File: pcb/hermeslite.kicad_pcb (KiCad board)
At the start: 4 copper layers, 48.8 x 51 mm, 71 parts, among them CN1 MEC6-140_CONNECTOR_BEMICRO, CN2 PCIE, P1 CONN_4, P10 CONN_1, P13 CONN_1, P14 CONN_1, P15 Si510 73.728, P16 CONN_3X2, P17 CONN_4, P18 CONN_1, P19 CONN_1, P2 CONN_1, P20 CONN_1, P22 CONN_1, P23 CONN_5, P24 CONN_5, P25 CONN_5, P3 CONN_1, P4 CONN_1, P5 CONN_1, P6 CONN_1, P8 CONN_1, P9 CONN_1, T1 TRANSF_ADT8, T2 TRANSF_ADT2, T3 TRANSF_ADT2, U1 AD9866BCPZ, U2 NCP1117ST33T3G, U3 NCP1117ST33T3G

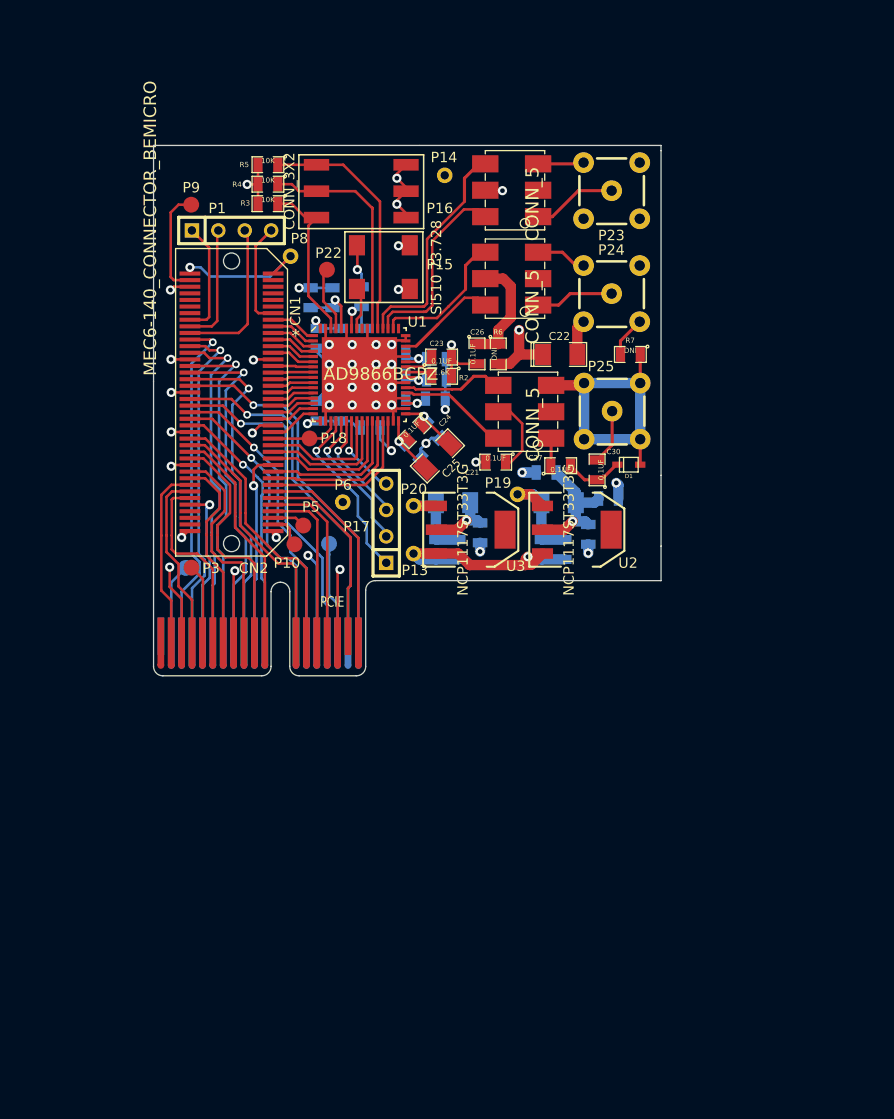
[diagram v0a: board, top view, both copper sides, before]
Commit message: RTL cleanup and upgrade to Quartus 14.0
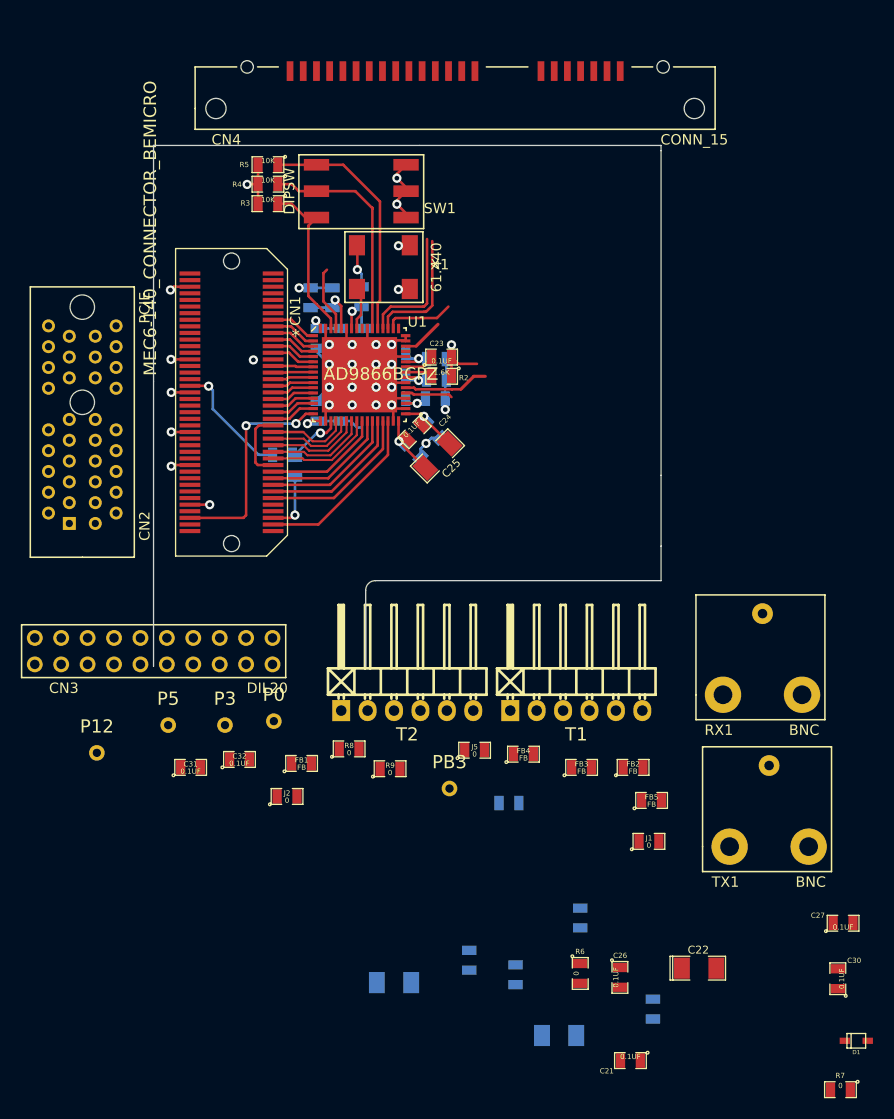
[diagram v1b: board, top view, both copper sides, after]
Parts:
- removed L1, L2, L3, L4: FB, SMD_Packages:SM0805
- removed P1, P17: CONN_4, Connect:SIL-4
- removed P10, P18, P2, P22, P4, P9: CONN_1, Measurement_Points:Measurement_Point_Round-SMD-Pad_Small
- removed P13, P14, P19, P20, P6, P8: CONN_1, Measurement_Points:Measurement_Point_Round-TH_Small
- removed P23, P24, P25: CONN_5, BEMICRO:SMA
- removed T3: TRANSF_ADT2, MINICKTS:minicircuits-CD542
- removed U2, U3: NCP1117ST33T3G, SMD_Packages:SOT223
- added C31: 0.1UF, SMD_Packages:SMD-0805, F.Cu at (104.3, 143.3)
- added C32: 0.1UF, SMD_Packages:SMD-0805, F.Cu at (109.0, 142.5)
- added CN3: DIL20, HERMESLITE:WAVESHARE, F.Cu at (89.3, 133.3)
- added CN4: CONN_15, HERMESLITE:SATA22, F.Cu at (129.7, 79.9)
- added FB1: FB, SMD_Packages:SMD-0805, F.Cu at (114.9, 142.9)
- added FB2: FB, SMD_Packages:SMD-0805, F.Cu at (146.8, 143.3)
- added FB3: FB, SMD_Packages:SMD-0805, F.Cu at (141.9, 143.3)
- added FB4: FB, SMD_Packages:SMD-0805, F.Cu at (136.3, 142.0)
- added FB5: FB, SMD_Packages:SMD-0805, F.Cu at (148.6, 146.4)
- added J1: 0, SMD_Packages:SMD-0805, F.Cu at (148.3, 150.4)
- added J2: 0, SMD_Packages:SMD-0805, F.Cu at (113.5, 146.1)
- added J3: 0, SMD_Packages:SMD-0805, B.Cu at (114.3, 114.4)
- added J4: 0, SMD_Packages:SMD-0805, B.Cu at (113.1, 113.2)
- added J5: 0, SMD_Packages:SMD-0805, F.Cu at (131.6, 141.6)
- added P0: CONN_1, Measurement_Points:Measurement_Point_Round-TH_Small, F.Cu at (112.3, 138.8)
- added P12: CONN_1, Measurement_Points:Measurement_Point_Round-TH_Small, F.Cu at (95.2, 141.9)
- added PB3: CONN_1, Measurement_Points:Measurement_Point_Round-TH_Small, F.Cu at (129.2, 145.3)
- added R8: 0, SMD_Packages:SMD-0805, F.Cu at (119.5, 141.5)
- added R9: 0, SMD_Packages:SMD-0805, F.Cu at (123.4, 143.4)
- added RX1: BNC, HERMESLITE:BNCRA, F.Cu at (159.3, 136.3)
- added TX1: BNC, HERMESLITE:BNCRA, F.Cu at (159.9, 150.9)
- CN2: footprint Connect:PCI-EXPRESS -> HERMESLITE:PCIE36
- P3, P5: footprint Measurement_Points:Measurement_Point_Round-SMD-Pad_Small -> Measurement_Points:Measurement_Point_Round-TH_Small
- R1: value 10K -> 200
- R6, R7: value DNI -> 0
- SW1: renamed from P16; value CONN_3X2 -> DIPSW
- T1: value TRANSF_ADT8 -> 8:1; footprint MINICKTS:minicircuits-CD542 -> Pin_Headers:Pin_Header_Angled_1x06
- T2: value TRANSF_ADT2 -> 4:1; footprint MINICKTS:minicircuits-CD542 -> Pin_Headers:Pin_Header_Angled_1x06
- X1: renamed from P15; value Si510 73.728 -> 61.440
- moved R7 73.5 mm to (166.8, 174.2)
- moved C26 61.5 mm to (145.5, 163.4)
- moved C22 60.5 mm to (153.2, 162.6)
- moved R6 60.1 mm to (141.7, 163.1)
- moved D1 59.6 mm to (168.3, 169.5)
- moved C21 59.0 mm to (146.6, 171.4)
- moved C30 54.1 mm to (166.5, 163.6)
- moved C27 51.7 mm to (167.0, 158.2)
- moved C19 51.2 mm to (139.7, 169.0)
- moved T2 49.5 mm to (125.1, 137.8), turned to 0 degrees
- moved C20 46.5 mm to (123.8, 164.0)
- moved C17 45.0 mm to (148.7, 166.5)
- moved C15 41.0 mm to (135.5, 163.2)
- moved C16 39.6 mm to (131.1, 161.8)
- moved R1 38.5 mm to (134.9, 146.7)
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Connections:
- C10 pad 2: GND -> Net-(C10-Pad2)
- C13 pad 2: GND -> Net-(C10-Pad2)
- C15 pad 1: VIN -> 3VIN
- C16 pad 1: VIN -> 3VIN
- C17 pad 1: VIN -> 3VIN
- C18 pad 1: VIN -> 3VIN
- C19 pad 1: Net-(C19-Pad1) -> 3VIN
- C20 pad 1: Net-(C20-Pad1) -> 3VIN
- C22 pad 1: VIN -> Net-(C22-Pad1)
- C23 pad 1: Net-(C23-Pad1) -> GND
- C23 pad 2: GND -> Net-(C23-Pad2)
- C28 pad 1: Net-(C24-Pad1) -> Net-(C24-Pad2)
- C29 pad 1: Net-(C24-Pad2) -> Net-(C24-Pad1)
- CN1 pad 78: Net-(CN1-Pad78) -> DVDD
- CN1 pad 79: Net-(CN1-Pad79) -> 5VIN
- CN1 pad 80: Net-(CN1-Pad79) -> 5VIN
- CN2 pad A1: Net-(CN2-PadA1) -> GND
- CN2 pad A11: Net-(CN1-Pad34) -> 12VIN
- CN2 pad A12: Net-(CN1-Pad36) -> 5VIN
- CN2 pad A13: Net-(CN1-Pad38) -> 3VIN
- CN2 pad A14: GND -> Net-(CN1-Pad66)
- CN2 pad A15: Net-(CN1-Pad40) -> Net-(CN1-Pad64)
- CN2 pad A16: Net-(CN2-PadA16) -> Net-(CN1-Pad62)
- CN2 pad A17: Net-(CN1-Pad42) -> Net-(CN1-Pad60)
- CN2 pad A18: Net-(CN1-Pad46) -> GND
- CN2 pad A2: Net-(CN2-PadA2) -> RXN
- CN2 pad A3: Net-(CN1-Pad60) -> RXP
- CN2 pad A4: Net-(CN1-Pad58) -> GND
- CN2 pad A5: GND -> TXN
- CN2 pad A6: Net-(CN1-Pad56) -> TXP
- CN2 pad A7: Net-(CN1-Pad52) -> GND
- CN2 pad A8: Net-(CN1-Pad50) -> TXLN
- CN2 pad A9: Net-(CN1-Pad48) -> TXLP
- CN2 pad B1: Net-(CN2-PadB1) -> GND
- CN2 pad B10: Net-(CN1-Pad24) -> GND
- CN2 pad B11: Net-(CN1-Pad26) -> 12VIN
- CN2 pad B12: Net-(CN1-Pad28) -> 5VIN
- CN2 pad B13: Net-(CN1-Pad30) -> 3VIN
- CN2 pad B14: Net-(CN1-Pad7) -> Net-(CN1-Pad50)
- CN2 pad B15: Net-(CN1-Pad9) -> Net-(CN1-Pad52)
- CN2 pad B16: GND -> Net-(CN1-Pad56)
- CN2 pad B17: Net-(CN1-Pad11) -> Net-(CN1-Pad58)
- CN2 pad B18: Net-(CN1-Pad13) -> GND
- CN2 pad B2: Net-(CN1-Pad16) -> GND
- CN2 pad B4: Net-(CN1-Pad14) -> GND
- CN2 pad B5: Net-(CN2-PadB5) -> GND
- CN2 pad B6: Net-(CN1-Pad12) -> GND
- CN2 pad B7: Net-(CN1-Pad18) -> GND
- CN2 pad B9: Net-(CN1-Pad20) -> GND
- D1 pad 1: Net-(D1-Pad1) -> GND
- P3 pad 1: Net-(CN2-PadB5) -> 3VIN
- P5 pad 1: Net-(CN1-Pad5) -> 5VIN
- R1 pad 1: DVDD -> TXP
- R1 pad 2: Net-(R1-Pad2) -> TXN
- R2 pad 1: GND -> Net-(R2-Pad1)
- R2 pad 2: Net-(R2-Pad2) -> GND
- R3 pad 1: Net-(P16-Pad2) -> Net-(R3-Pad1)
- R4 pad 1: Net-(P16-Pad4) -> Net-(R4-Pad1)
- R5 pad 1: Net-(P16-Pad6) -> Net-(R5-Pad1)
- R6 pad 2: VIN -> Net-(C22-Pad1)
- R7 pad 1: Net-(D1-Pad1) -> DVDD
- R7 pad 2: GND -> Net-(R5-Pad1)
- SW1 pad 1: DVDD -> Net-(R5-Pad1)
- SW1 pad 2: Net-(P16-Pad2) -> DVDD
- SW1 pad 3: DVDD -> Net-(R4-Pad1)
- SW1 pad 4: Net-(P16-Pad4) -> DVDD
- SW1 pad 5: DVDD -> Net-(R3-Pad1)
- SW1 pad 6: Net-(P16-Pad6) -> DVDD
- T1 pad 3: Net-(D1-Pad1) -> GND
- T1 pad 4: RXP -> Net-(C32-Pad1)
- T1 pad 6: RXN -> Net-(C31-Pad1)
- T2 pad 4: Net-(T2-Pad4) -> TXP
- T2 pad 5: GND -> Net-(C26-Pad1)
- T2 pad 6: Net-(T2-Pad6) -> TXN
- U1 pad 16: Net-(CN1-Pad31) -> Net-(CN1-Pad6)
- U1 pad 19: Net-(CN1-Pad29) -> Net-(J3-Pad1)
- U1 pad 20: SDIO -> Net-(CN1-Pad31)
- U1 pad 21: SDO -> Net-(CN1-Pad29)
- U1 pad 22: SCLK -> Net-(CN1-Pad27)
- U1 pad 23: SEN -> Net-(CN1-Pad25)
- U1 pad 24: Net-(CN1-Pad27) -> Net-(CN1-Pad23)
- U1 pad 25: Net-(CN1-Pad25) -> Net-(CN1-Pad19)
- U1 pad 26: Net-(CN1-Pad23) -> Net-(CN1-Pad17)
- U1 pad 27: Net-(CN1-Pad19) -> Net-(CN1-Pad15)
- U1 pad 28: Net-(CN1-Pad17) -> Net-(CN1-Pad13)
- U1 pad 29: Net-(CN1-Pad15) -> Net-(CN1-Pad11)
- U1 pad 30: Net-(R1-Pad2) -> Net-(CN1-Pad3)
- U1 pad 32: Net-(C24-Pad2) -> Net-(C24-Pad1)
- U1 pad 33: Net-(C24-Pad1) -> Net-(C24-Pad2)
- U1 pad 41: Net-(R2-Pad2) -> Net-(R2-Pad1)
- U1 pad 42: Net-(C23-Pad1) -> Net-(C23-Pad2)
- U1 pad 46: Net-(T3-Pad6) -> TXN
- U1 pad 50: Net-(T3-Pad4) -> TXP
- U1 pad 51: Net-(T2-Pad6) -> TXLN
- U1 pad 52: Net-(T2-Pad4) -> TXLP
- U1 pad 53: Net-(P16-Pad6) -> Net-(R5-Pad1)
- U1 pad 54: Net-(P16-Pad4) -> Net-(R4-Pad1)
- U1 pad 62: Net-(P16-Pad2) -> Net-(R3-Pad1)
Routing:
- net GND: track 281.2 -> 173.8 mm, vias 38 -> 28
- net Net-(CN1-Pad42): track 34.2 -> 0.00 mm, vias 1 -> 0
- net Net-(CN1-Pad50): track 33.1 -> 0.00 mm, vias 1 -> 0
- net Net-(CN1-Pad60): track 33.0 -> 0.00 mm, vias 1 -> 0
- net Net-(CN1-Pad52): track 32.8 -> 0.00 mm, vias 1 -> 0
- net Net-(CN1-Pad58): track 32.7 -> 0.00 mm, vias 1 -> 0
- net DVDD: track 24.4 -> 57.1 mm, vias 6 -> 3
- net Net-(CN1-Pad56): track 32.6 -> 0.00 mm, vias 1 -> 0
- net Net-(CN1-Pad40): track 32.4 -> 0.00 mm, vias 1 -> 0
- net Net-(CN1-Pad48): track 32.1 -> 0.00 mm, vias 1 -> 0
- net Net-(D1-Pad1): track 30.1 -> 0.00 mm
- net VIN: track 29.4 -> 0.00 mm, vias 2 -> 0
- net Net-(CN1-Pad38): track 28.3 -> 0.00 mm, vias 1 -> 0
- net Net-(CN1-Pad36): track 27.5 -> 0.00 mm, vias 1 -> 0
- net Net-(CN1-Pad30): track 26.0 -> 0.00 mm
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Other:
- board size 48.8 x 51 mm -> 48.8 x 50.1 mm

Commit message: Intermediate save before move of PCIe connector
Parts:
- removed CN3: DIL20, HERMESLITE:WAVESHARE
- removed R6, R7: 0, SMD_Packages:SM0805
- removed R8, R9: 0, SMD_Packages:SMD-0805
- removed SW1: DIPSW, HERMESLITE:DIPSWITCH
- added C33: 0.1UF, SMD_Packages:SMD-0805, B.Cu at (104.8, 108.4)
- added MH: VAL**, HERMESLITE:MH, F.Cu at (116.7, 122.8)
- added MH: VAL**, HERMESLITE:MH, F.Cu at (108.3, 87.1)
- added MH: VAL**, HERMESLITE:MH, F.Cu at (146.7, 87.1)
- added MH: VAL**, HERMESLITE:MH, F.Cu at (146.7, 122.8)
- added TP1: CONN_1, HERMESLITE:TP, F.Cu at (102.1, 108.4)
- added TP2: CONN_1, HERMESLITE:TP, F.Cu at (114.1, 99.3)
- added U2: EEPROM, SMD_Packages:SOT-23-6, B.Cu at (105.1, 111.9)
- C15, C16, C17, C18, R1: footprint SMD_Packages:SM0805 -> SMD_Packages:SMD-0805; moved to F.Cu
- C19, C20: footprint SMD_Packages:SM1206POL -> SMD_Packages:SMD-1206_Pol; moved to F.Cu
- C21, C26, C27, C30: footprint SMD_Packages:SM0805 -> SMD_Packages:SMD-0805; moved to B.Cu
- C22: footprint SMD_Packages:SM1206POL -> SMD_Packages:SMD-1206_Pol; moved to B.Cu
- CN2: footprint HERMESLITE:PCIE36 -> HERMESLITE:PCIESTRADDLE
- CN4: value CONN_15 -> SATA22; moved to B.Cu
- D1, FB5: moved to B.Cu
- R3: value 10K -> 0; footprint SMD_Packages:SM0805 -> SMD_Packages:SMD-0805; moved to B.Cu
- R4, R5: value 10K -> 47; footprint SMD_Packages:SM0805 -> SMD_Packages:SMD-0805; moved to B.Cu
- RX1, TX1: value BNC -> ~; footprint HERMESLITE:BNCRA -> HERMESLITE:RFSTRADDLE; moved to B.Cu
- T1, T2: footprint Pin_Headers:Pin_Header_Angled_1x06 -> HERMESLITE:TRANSF
- moved C22 69.9 mm to (141.0, 93.7)
- moved C26 66.9 mm to (141.2, 96.7), turned to 90 degrees
- moved C21 65.3 mm to (142.4, 106.3), turned to 90 degrees
- moved D1 65.0 mm to (142.4, 109.9), turned to 90 degrees
- moved C30 55.8 mm to (143.3, 112.8), turned to 0 degrees
- moved TX1 55.1 mm to (147.8, 97.1)
- moved FB5 54.1 mm to (136.4, 93.7)
- moved J1 54.0 mm to (129.0, 100.0), turned to 270 degrees
- moved C27 52.3 mm to (139.1, 114.0)
- moved CN4 51.9 mm to (125.7, 131.6), turned to 180 degrees
- moved R1 48.4 mm to (131.0, 98.4), turned to 270 degrees
- moved CN2 48.1 mm to (122.3, 85.3), turned to 0 degrees
- moved P12 47.6 mm to (135.9, 117.1)
- moved J2 47.4 mm to (131.0, 102.0), turned to 270 degrees
- moved C31 44.7 mm to (132.0, 108.2), turned to 180 degrees
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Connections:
- C21 pad 1: Net-(C21-Pad1) -> GND
- C21 pad 2: GND -> Net-(C21-Pad2)
- C31 pad 1: Net-(C31-Pad1) -> RXN
- C31 pad 2: RXN -> Net-(C31-Pad2)
- C32 pad 1: Net-(C32-Pad1) -> RXP
- C32 pad 2: RXP -> Net-(C32-Pad2)
- CN1 pad 10: GND -> Net-(C33-Pad1)
- CN1 pad 22: GND -> Net-(C33-Pad1)
- CN1 pad 32: GND -> Net-(C33-Pad1)
- CN1 pad 4: Net-(CN1-Pad4) -> GND
- CN1 pad 44: GND -> Net-(C33-Pad1)
- CN1 pad 54: GND -> Net-(C33-Pad1)
- CN1 pad 76: GND -> Net-(C33-Pad1)
- CN2 pad A12: 5VIN -> 12VIN
- CN2 pad A13: 3VIN -> 5VIN
- CN2 pad A14: Net-(CN1-Pad66) -> 5VIN
- CN2 pad A15: Net-(CN1-Pad64) -> 3VIN
- CN2 pad A16: Net-(CN1-Pad62) -> 3VIN
- CN2 pad A17: Net-(CN1-Pad60) -> GND
- CN2 pad A2: RXN -> GND
- CN2 pad A3: RXP -> GND
- CN2 pad A5: TXN -> GND
- CN2 pad A6: TXP -> GND
- CN2 pad A8: TXLN -> GND
- CN2 pad A9: TXLP -> GND
- CN2 pad B11: 12VIN -> Net-(CN1-Pad50)
- CN2 pad B12: 5VIN -> Net-(CN1-Pad52)
- CN2 pad B13: 3VIN -> Net-(CN1-Pad56)
- CN2 pad B14: Net-(CN1-Pad50) -> Net-(CN1-Pad58)
- CN2 pad B15: Net-(CN1-Pad52) -> Net-(CN1-Pad66)
- CN2 pad B16: Net-(CN1-Pad56) -> Net-(CN1-Pad64)
- CN2 pad B17: Net-(CN1-Pad58) -> Net-(CN1-Pad62)
- CN2 pad B18: GND -> Net-(CN1-Pad60)
- CN2 pad B2: GND -> RXN
- CN2 pad B3: GND -> RXP
- CN2 pad B5: GND -> TXN
- CN2 pad B6: GND -> TXP
- CN2 pad B8: GND -> TXLN
- CN2 pad B9: GND -> TXLP
- CN4 pad P1: (no net) -> 3VIN
- CN4 pad P10: (no net) -> GND
- CN4 pad P11: (no net) -> GND
- CN4 pad P12: (no net) -> GND
- CN4 pad P13: (no net) -> 12VIN
- CN4 pad P14: (no net) -> 12VIN
- CN4 pad P15: (no net) -> 12VIN
- CN4 pad P2: (no net) -> 3VIN
- CN4 pad P3: (no net) -> 3VIN
- CN4 pad P4: (no net) -> GND
- CN4 pad P5: (no net) -> GND
- CN4 pad P6: (no net) -> GND
- CN4 pad P7: (no net) -> 5VIN
- CN4 pad P8: (no net) -> 5VIN
- CN4 pad P9: (no net) -> 5VIN
- CN4 pad S1: (no net) -> GND
- CN4 pad S2: (no net) -> Net-(CN1-Pad12)
- CN4 pad S3: (no net) -> Net-(CN1-Pad14)
- CN4 pad S4: (no net) -> GND
- CN4 pad S5: (no net) -> Net-(CN1-Pad16)
- CN4 pad S6: (no net) -> Net-(CN1-Pad18)
- CN4 pad S7: (no net) -> GND
- D1 pad 1: GND -> Net-(C27-Pad2)
- D1 pad 2: Net-(C27-Pad2) -> GND
- J5 pad 1: Net-(CN1-Pad4) -> GND
- R3 pad 1: Net-(R3-Pad1) -> Net-(C26-Pad1)
- R3 pad 2: GND -> Net-(C22-Pad1)
- R4 pad 1: Net-(R4-Pad1) -> Net-(CN1-Pad6)
- R5 pad 1: Net-(R5-Pad1) -> GND
- R5 pad 2: GND -> Net-(J3-Pad1)
- T1 pad 2: (no net) -> Net-(C21-Pad2)
- T1 pad 4: Net-(C32-Pad1) -> RXP
- T1 pad 5: Net-(C21-Pad1) -> Net-(C21-Pad2)
- T1 pad 6: Net-(C31-Pad1) -> RXN
- T2 pad 2: (no net) -> Net-(C26-Pad1)
- U1 pad 37: RXN -> Net-(C31-Pad2)
- U1 pad 38: RXP -> Net-(C32-Pad2)
- U1 pad 53: Net-(R5-Pad1) -> GND
- U1 pad 54: Net-(R4-Pad1) -> GND
- U1 pad 62: Net-(R3-Pad1) -> GND
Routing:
- net DVDD: track 57.1 -> 17.7 mm, vias 3 -> 4
- net GND: track 173.8 -> 195.1 mm, vias 28 -> 25
- net Net-(CN1-Pad18): track 0.00 -> 19.7 mm, vias 0 -> 1
- net Net-(CN1-Pad16): track 0.00 -> 18.3 mm, vias 0 -> 1
- net Net-(CN1-Pad14): track 0.00 -> 18.2 mm, vias 0 -> 1
- net Net-(C33-Pad1): track 0.00 -> 16.8 mm, vias 0 -> 6
- net Net-(CN1-Pad12): track 0.00 -> 16.4 mm, vias 0 -> 1
- net Net-(R4-Pad1): track 16.1 -> 0.00 mm, vias 1 -> 0
- net Net-(CN1-Pad1): track 0.18 -> 11.2 mm
- net RXP: track 8.24 -> 0.00 mm
- net Net-(R5-Pad1): track 7.81 -> 0.00 mm
- net Net-(CN1-Pad34): track 0.00 -> 7.50 mm, vias 0 -> 1
- net Net-(C31-Pad2): track 0.00 -> 6.58 mm
- net Net-(J2-Pad2): track 0.00 -> 6.55 mm
- net Net-(C32-Pad2): track 0.00 -> 6.50 mm
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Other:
- board size 48.8 x 50.1 mm -> 49.9 x 49.9 mm

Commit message: Commit before silkscreen cleanup
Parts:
- removed D1: CDSOD323, HERMESLITE:SOD323
- removed R3: 0, SMD_Packages:SMD-0805
- removed RX1, TX1: ~, HERMESLITE:RFSTRADDLE
- removed T1: 8:1, HERMESLITE:TRANSF
- removed T2: 4:1, HERMESLITE:TRANSF
- added C34: 0.1UF, SMD_Packages:SMD-0805, B.Cu at (141.2, 90.4)
- added C35: 0.1UF, SMD_Packages:SMD-0805, B.Cu at (137.2, 90.4)
- added C36: 0.1UF, SMD_Packages:SMD-0805, B.Cu at (142.3, 122.5)
- added FB6: FB, SMD_Packages:SMD-0805, B.Cu at (139.5, 96.6)
- added FB7: FB, SMD_Packages:SMD-0805, B.Cu at (137.4, 96.6)
- added FB8: FB, SMD_Packages:SMD-0805, B.Cu at (140.1, 102.1)
- added R6: 200, SMD_Packages:SMD-0805, F.Cu at (128.2, 98.1)
- C21, C26, C27, C30: value 0.1UF -> 1UF
- C22: value 10UF -> 0.1UF; footprint SMD_Packages:SMD-1206_Pol -> SMD_Packages:SMD-0805
- moved C17 32.8 mm to (138.1, 122.0), turned to 90 degrees
- moved C21 31.8 mm to (115.7, 89.1)
- moved CN2 29.9 mm to (146.5, 102.9), turned to 270 degrees
- moved C22 27.6 mm to (113.8, 89.1), turned to 90 degrees
- moved C15 26.9 mm to (136.1, 122.0), turned to 90 degrees
- moved C19 26.0 mm to (140.4, 121.3), turned to 90 degrees
- moved C27 23.9 mm to (135.2, 90.4), turned to 90 degrees
- moved C18 23.4 mm to (123.8, 122.0), turned to 90 degrees
- moved FB5 22.6 mm to (113.8, 93.1), turned to 270 degrees
- moved C20 22.2 mm to (121.5, 121.3), turned to 90 degrees
- moved C16 20.2 mm to (125.8, 122.0), turned to 90 degrees
- moved FB3 11.0 mm to (134.1, 122.0), turned to 90 degrees
- moved C30 10.1 mm to (140.4, 122.5), turned to 90 degrees
- moved P12 9.44 mm to (140.2, 125.5)
- moved C26 6.61 mm to (139.2, 90.4)
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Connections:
- net Net-(CN1-Pad56) renamed /EXP_GPIO1
- net Net-(CN1-Pad58) renamed /EXP_GPIO2
- net RXN renamed /RXN
- net RXP renamed /RXP
- net TXLN renamed /TXLN
- net TXLP renamed /TXLP
- net TXN renamed /TXN
- net TXP renamed /TXP
- C10 pad 2: Net-(C10-Pad2) -> GND
- C13 pad 2: Net-(C10-Pad2) -> GND
- C21 pad 1: GND -> 5VIN
- C21 pad 2: Net-(C21-Pad2) -> GND
- C22 pad 1: Net-(C22-Pad1) -> 5VIN
- C23 pad 1: GND -> Net-(C23-Pad1)
- C23 pad 2: Net-(C23-Pad2) -> GND
- C26 pad 1: Net-(C26-Pad1) -> DVDD
- C27 pad 1: Net-(C27-Pad1) -> 5VIN
- C27 pad 2: Net-(C27-Pad2) -> GND
- C28 pad 1: Net-(C24-Pad2) -> Net-(C24-Pad1)
- C29 pad 1: Net-(C24-Pad1) -> Net-(C24-Pad2)
- C30 pad 1: Net-(C27-Pad2) -> 12VIN
- C30 pad 2: Net-(C30-Pad2) -> GND
- C33 pad 1: Net-(C33-Pad1) -> GND
- CN1 pad 10: Net-(C33-Pad1) -> GND
- CN1 pad 22: Net-(C33-Pad1) -> GND
- CN1 pad 32: Net-(C33-Pad1) -> GND
- CN1 pad 44: Net-(C33-Pad1) -> GND
- CN1 pad 50: Net-(CN1-Pad50) -> /PTT#
- CN1 pad 52: Net-(CN1-Pad52) -> /EXP_GPIO0
- CN1 pad 54: Net-(C33-Pad1) -> GND
- CN1 pad 60: Net-(CN1-Pad60) -> /EXP_SEN
- CN1 pad 62: Net-(CN1-Pad62) -> /EXP_SDI
- CN1 pad 64: Net-(CN1-Pad64) -> /EXP_SDO
- CN1 pad 66: Net-(CN1-Pad66) -> /EXP_SCLK
- CN1 pad 73: Net-(CN1-Pad73) -> /PTT#
- CN1 pad 75: Net-(CN1-Pad75) -> /EXP_GPIO0
- CN1 pad 76: Net-(C33-Pad1) -> GND
- CN1 pad 79: 5VIN -> FPGA5V
- CN1 pad 80: 5VIN -> FPGA5V
- CN2 pad A11: 12VIN -> EXP12V
- CN2 pad A12: 12VIN -> EXP12V
- CN2 pad A13: 5VIN -> EXP5V
- CN2 pad A14: 5VIN -> EXP5V
- CN2 pad A15: 3VIN -> EXP3V
- CN2 pad A16: 3VIN -> EXP3V
- CN2 pad B11: Net-(CN1-Pad50) -> /PTT#
- CN2 pad B12: Net-(CN1-Pad52) -> /EXP_GPIO0
- CN2 pad B15: Net-(CN1-Pad66) -> /EXP_SEN
- CN2 pad B16: Net-(CN1-Pad64) -> /EXP_SDI
- CN2 pad B17: Net-(CN1-Pad62) -> /EXP_SDO
- CN2 pad B18: Net-(CN1-Pad60) -> /EXP_SCLK
- FB5 pad 2: Net-(C22-Pad1) -> FPGA5V
- R2 pad 1: Net-(R2-Pad1) -> GND
- R2 pad 2: GND -> Net-(R2-Pad2)
- U1 pad 32: Net-(C24-Pad1) -> Net-(C24-Pad2)
- U1 pad 33: Net-(C24-Pad2) -> Net-(C24-Pad1)
- U1 pad 41: Net-(R2-Pad1) -> Net-(R2-Pad2)
- U1 pad 42: Net-(C23-Pad2) -> Net-(C23-Pad1)
- U2 pad 2: Net-(C33-Pad1) -> GND
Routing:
- net GND: track 195.1 -> 288.1 mm, vias 25 -> 49
- net 5VIN: track 0.01 -> 82.3 mm, vias 0 -> 2
- net /PTT#: track 0.00 -> 54.1 mm
- net /EXP_GPIO0: track 0.00 -> 52.3 mm
- net /EXP_SDI: track 0.00 -> 51.3 mm
- net /EXP_GPIO1: track 0.00 -> 51.1 mm
- net /EXP_SDO: track 0.00 -> 51.1 mm
- net /EXP_GPIO2: track 0.00 -> 50.9 mm
- net /EXP_SCLK: track 0.00 -> 50.9 mm
- net /EXP_SEN: track 0.00 -> 50.6 mm
- net 3VIN: track 0.00 -> 32.8 mm
- net /TXP: track 6.55 -> 27.0 mm
- net DVDD: track 17.7 -> 36.7 mm, vias 4 -> 7
- net Net-(C33-Pad1): track 16.8 -> 0.00 mm, vias 6 -> 0
- net /TXN: track 6.76 -> 23.3 mm
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- added copper zone on Inner1.Cu, net 12VIN
- added copper zone on Inner1.Cu, net 5VIN
- added copper zone on B.Cu, net GND
- added copper zone on F.Cu, net GND
- removed copper zone on Inner1.Cu, net VIN
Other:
- outline, holes or cut-outs redrawn
- board text added: "Hermes-Lite 1.2 Copyright 2014 SofterHardware"
- board text removed: "SDR Rev 0.9 Copyright 2014 SofterHardware"

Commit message: Version 1.2 for review
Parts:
- P3: value CONN_1 -> 3V
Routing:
- net GND: track 288.1 -> 299.9 mm
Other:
- board text added: "12V"
- board text added: "3V"
- board text added: "5V"
- board text added: "F3V"
- board text added: "GND"
